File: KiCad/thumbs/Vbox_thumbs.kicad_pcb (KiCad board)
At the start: 2 copper layers, 33.1 x 114.3 mm, 4 parts, among them J4 Conn_01x06, J5 Conn_01x06, J6 Conn_01x10, J7 Conn_01x10

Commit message: thumbs and fingers
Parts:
- removed J4, J5: Conn_01x06, Connector_JST:JST_PH_S6B-PH-SM4-TB_1x06-1MP_P2.00mm_Horizontal
- removed J6, J7: Conn_01x10, Connector_JST:JST_PH_S10B-PH-SM4-TB_1x10-1MP_P2.00mm_Horizontal
- added J1: Conn_01x06, Connector_JST:JST_PH_S6B-PH-SM4-TB_1x06-1MP_P2.00mm_Horizontal, F.Cu at (85.2, 108.0)
- added J2: Conn_01x06, Connector_JST:JST_PH_S6B-PH-SM4-TB_1x06-1MP_P2.00mm_Horizontal, B.Cu at (85.2, 108.0)
- added SW1: SW_Push_45deg, Buttons:Vbox, F.Cu at (119.0, 109.5)
- added SW10: SW_Push_45deg, Buttons:Vbox, B.Cu at (138.0, 119.0)
- added SW2: SW_Push_45deg, Buttons:Vbox, F.Cu at (100.0, 100.0)
- added SW3: SW_Push_45deg, Buttons:Vbox, F.Cu at (119.0, 90.5)
- added SW4: SW_Push_45deg, Buttons:Vbox, F.Cu at (138.0, 100.0)
- added SW5: SW_Push_45deg, Buttons:Vbox, F.Cu at (138.0, 119.0)
- added SW6: SW_Push_45deg, Buttons:Vbox, B.Cu at (119.0, 109.5)
- added SW7: SW_Push_45deg, Buttons:Vbox, B.Cu at (100.0, 100.0)
- added SW8: SW_Push_45deg, Buttons:Vbox, B.Cu at (119.0, 90.5)
- added SW9: SW_Push_45deg, Buttons:Vbox, B.Cu at (138.0, 100.0)
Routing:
- net C_UP: track 0.00 -> 86.0 mm
- net C_DN: track 0.00 -> 65.7 mm
- net C_LT: track 0.00 -> 58.8 mm
- net M2: track 0.00 -> 56.2 mm
- net M3: track 0.00 -> 52.6 mm
- net M4: track 0.00 -> 44.7 mm
- net A: track 0.00 -> 33.8 mm
- net M1: track 0.00 -> 31.3 mm
- net C_RT: track 0.00 -> 17.0 mm
- net M5: track 0.00 -> 12.9 mm
- net GND: vias 32 -> 12
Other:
- board size 33.1 x 114.3 mm -> 67 x 46.5 mm

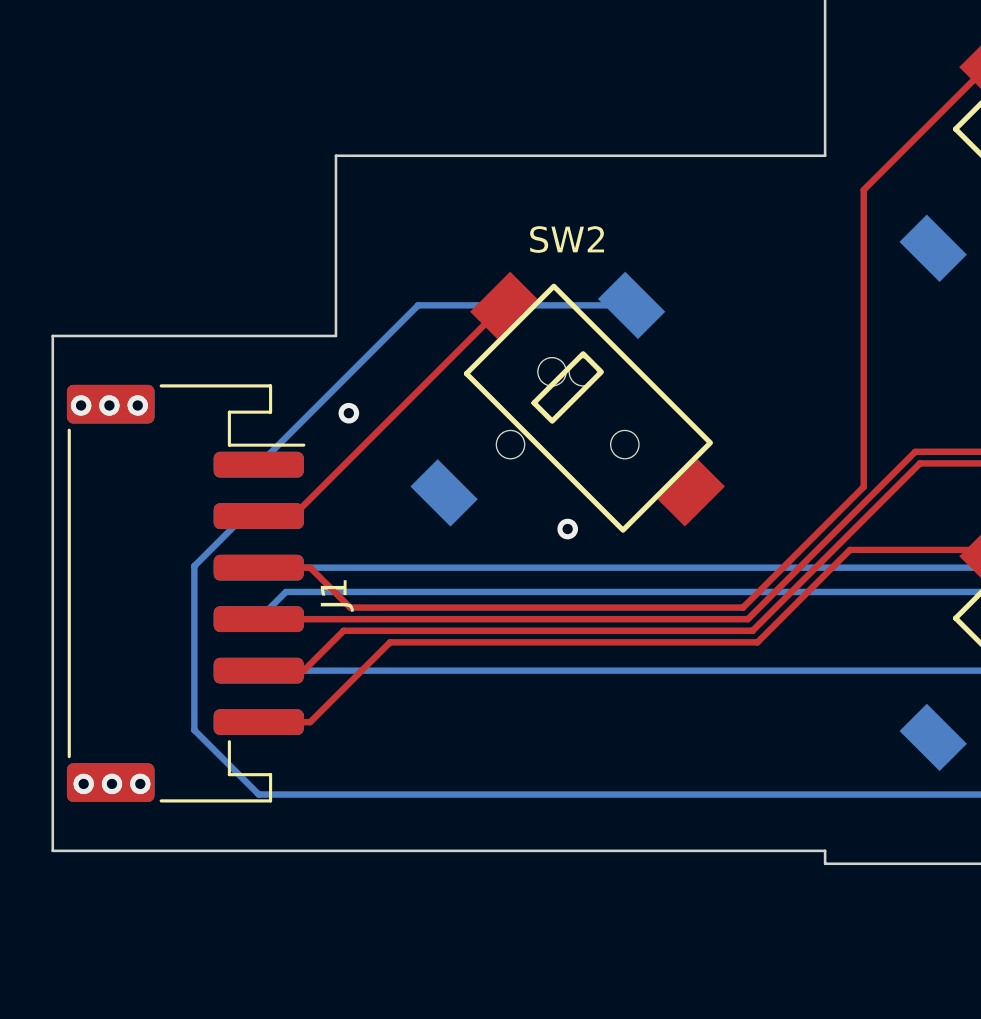
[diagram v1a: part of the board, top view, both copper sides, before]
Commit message: tweak outlines of button clusters
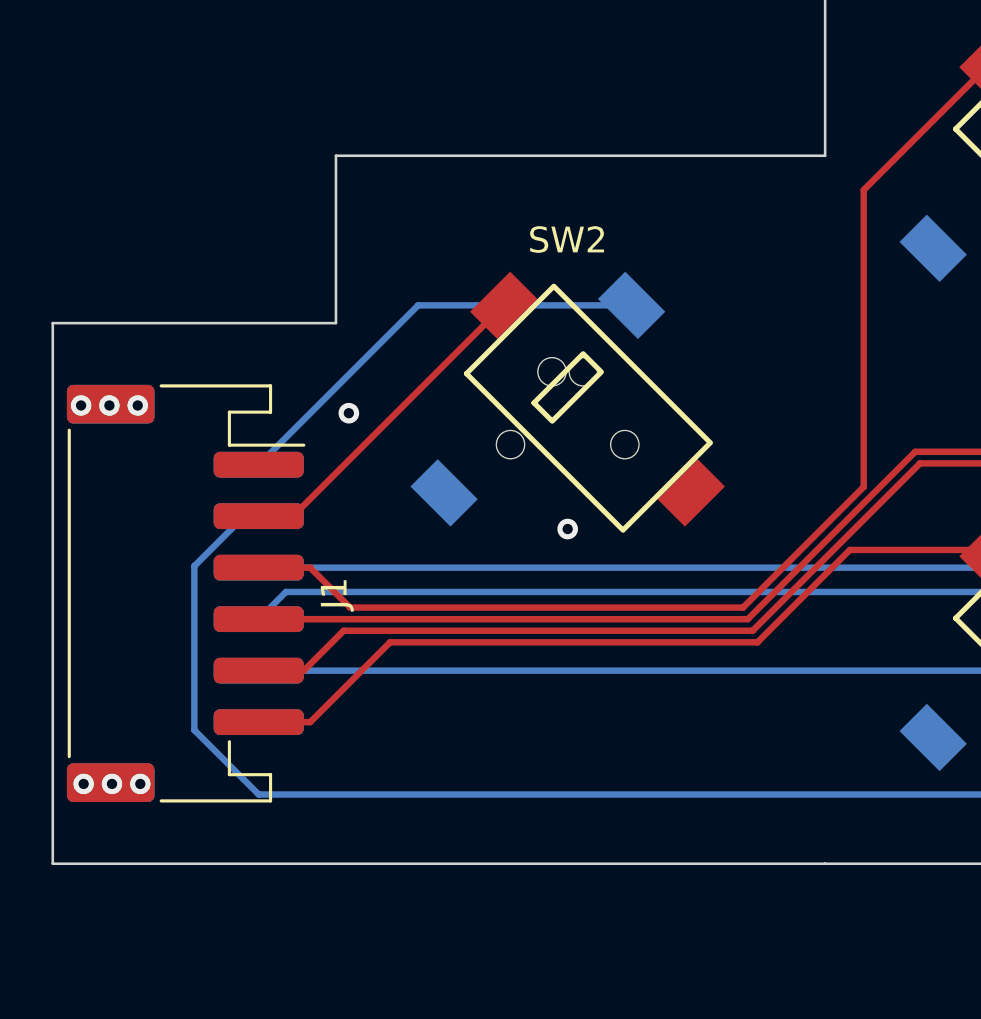
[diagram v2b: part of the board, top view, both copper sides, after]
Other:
- outline, holes or cut-outs redrawn
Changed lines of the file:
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@@
   (gr_poly
     (pts
-      (xy 80 118)
-      (xy 110 118)
+      (xy 80 118.5)
       (xy 110 118.5)
       (xy 129 118.5)
@@
       (xy 110 91)
       (xy 91 91)
-      (xy 91 98)
-      (xy 80 98)
+      (xy 91 97.5)
+      (xy 80 97.5)
     )
     (stroke (width 0.1) (type solid)) (fill none) (layer "Edge.Cuts"))
   (gr_text_box "VBox Thumb Cluster\nby CarVac\nLicense: CERN-OHL-S V2\ngithub.com/CarVac/vbox"
-    (start 90.5 109.5) (end 109.5 118) (layer "F.SilkS")
+    (start 90.5 111) (end 109.5 117.5) (layer "F.SilkS")
       (effects (font (size 0.8 0.8) (thickness 0.15)) (justify top))
   )
@@
     (polygon
       (pts
-        (xy 80 118)
-        (xy 110 118)
+        (xy 80 118.5)
         (xy 110 118.5)
         (xy 129 118.5)
@@
         (xy 110 91)
         (xy 91 91)
-        (xy 91 98)
-        (xy 80 98)
+        (xy 91 97.5)
+        (xy 80 97.5)
       )
     )
@@
     (polygon
       (pts
-        (xy 80 118)
-        (xy 110 118)
+        (xy 80 118.5)
         (xy 110 118.5)
         (xy 129 118.5)
@@
         (xy 110 91)
         (xy 91 91)
-        (xy 91 98)
-        (xy 80 98)
+        (xy 91 97.5)
+        (xy 80 97.5)
       )
     )

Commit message: fix drc errors
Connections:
- J2 pad 1: GND -> C_RT
- J2 pad 2: C_UP -> C_DN
- J2 pad 3: C_LT -> A
- J2 pad 4: A -> C_LT
- J2 pad 5: C_DN -> C_UP
- J2 pad 6: C_RT -> GND
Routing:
- net C_UP: track 86.0 -> 48.4 mm
- net C_RT: track 17.0 -> 33.2 mm
- net C_DN: track 65.7 -> 55.1 mm
- net C_LT: track 58.8 -> 56.7 mm
- net A: track 33.8 -> 34.6 mm
- net GND: vias 12 -> 11

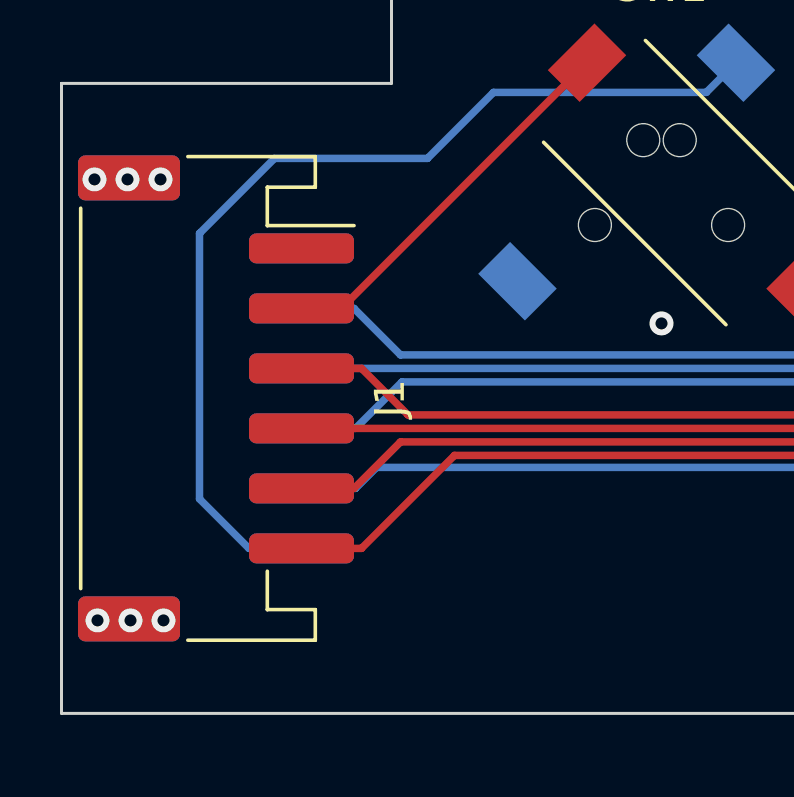
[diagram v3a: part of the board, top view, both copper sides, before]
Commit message: add thermal clearances to fingers, a few more vias
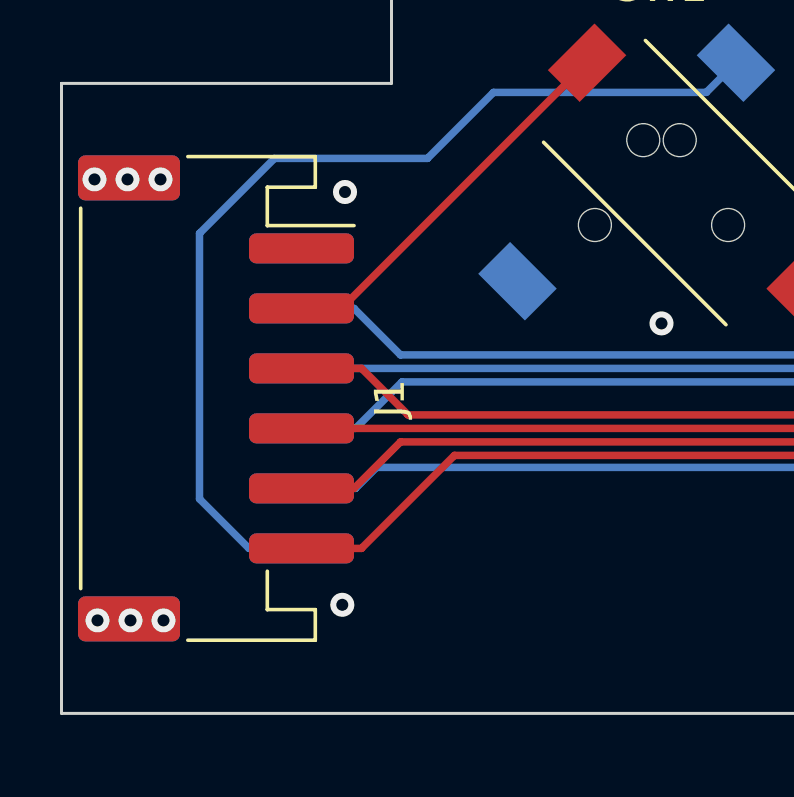
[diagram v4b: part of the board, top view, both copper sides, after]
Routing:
- net GND: vias 11 -> 13
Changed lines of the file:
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@@
       (net 4 "M5") (pinfunction "1") (pintype "passive"))
     (pad "2" smd rect (at 4.801256 4.094149 45) (size 2.2 1.5) (layers "F.Cu" "F.Paste" "F.Mask")
-      (net 1 "GND") (pinfunction "2") (pintype "passive"))
+      (net 1 "GND") (pinfunction "2") (pintype "passive") (thermal_gap 1))
   )
   (footprint "Buttons:Vbox" (layer "F.Cu")
@@
       (net 2 "M3") (pinfunction "1") (pintype "passive"))
     (pad "2" smd rect (at 4.801256 4.094149 45) (size 2.2 1.5) (layers "F.Cu" "F.Paste" "F.Mask")
-      (net 1 "GND") (pinfunction "2") (pintype "passive"))
+      (net 1 "GND") (pinfunction "2") (pintype "passive") (thermal_gap 1))
   )
   (footprint "Buttons:Vbox" (layer "F.Cu")
@@
       (net 5 "M1") (pinfunction "1") (pintype "passive"))
     (pad "2" smd rect (at 4.801256 4.094149 45) (size 2.2 1.5) (layers "F.Cu" "F.Paste" "F.Mask")
-      (net 1 "GND") (pinfunction "2") (pintype "passive"))
+      (net 1 "GND") (pinfunction "2") (pintype "passive") (thermal_gap 1))
   )
   (footprint "Buttons:Vbox" (layer "F.Cu")
@@
       (net 3 "M4") (pinfunction "1") (pintype "passive"))
     (pad "2" smd rect (at 4.801256 4.094149 45) (size 2.2 1.5) (layers "F.Cu" "F.Paste" "F.Mask")
-      (net 1 "GND") (pinfunction "2") (pintype "passive"))
+      (net 1 "GND") (pinfunction "2") (pintype "passive") (thermal_gap 1))
   )
   (footprint "Buttons:Vbox" (layer "F.Cu")
@@
       (net 6 "M2") (pinfunction "1") (pintype "passive"))
     (pad "2" smd rect (at 4.801256 4.094149 45) (size 2.2 1.5) (layers "F.Cu" "F.Paste" "F.Mask")
-      (net 1 "GND") (pinfunction "2") (pintype "passive"))
+      (net 1 "GND") (pinfunction "2") (pintype "passive") (thermal_gap 1))
   )
   (footprint "Connector_JST:JST_PH_S6B-PH-SM4-TB_1x06-1MP_P2.00mm_Horizontal" (layer "F.Cu")
@@
       (stroke (width 0.1) (type solid)) (layer "F.Fab"))
     (pad "1" smd roundrect (at -5 -2.85 270) (size 1 3.5) (layers "F.Cu" "F.Paste" "F.Mask") (roundrect_rratio 0.25)
-      (net 1 "GND") (pinfunction "Pin_1") (pintype "passive"))
+      (net 1 "GND") (pinfunction "Pin_1") (pintype "passive") (thermal_bridge_width 0.2) (thermal_gap 0.7))
     (pad "2" smd roundrect (at -3 -2.85 270) (size 1 3.5) (layers "F.Cu" "F.Paste" "F.Mask") (roundrect_rratio 0.25)
       (net 4 "M5") (pinfunction "Pin_2") (pintype "passive"))
@@
       (net 5 "M1") (pinfunction "Pin_6") (pintype "passive"))
     (pad "MP" smd roundrect (at -7.35 2.9 270) (size 1.5 3.4) (layers "F.Cu" "F.Paste" "F.Mask") (roundrect_rratio 0.166667)
-      (net 1 "GND"))
+      (net 1 "GND") (thermal_gap 1))
     (pad "MP" smd roundrect (at 7.35 2.9 270) (size 1.5 3.4) (layers "F.Cu" "F.Paste" "F.Mask") (roundrect_rratio 0.166667)
-      (net 1 "GND"))
+      (net 1 "GND") (thermal_gap 1))
     (model "${KICAD6_3DMODEL_DIR}/Connector_JST.3dshapes/JST_PH_S6B-PH-SM4-TB_1x06-1MP_P2.00mm_Horizontal.wrl"
       (offset (xyz 0 0 0))
@@
       (net 8 "C_LT") (pinfunction "1") (pintype "passive"))
     (pad "2" smd rect (at 4.801256 -4.094149 135) (size 2.2 1.5) (layers "B.Cu" "B.Paste" "B.Mask")
-      (net 1 "GND") (pinfunction "2") (pintype "passive"))
+      (net 1 "GND") (pinfunction "2") (pintype "passive") (thermal_gap 1))
   )
   (footprint "Buttons:Vbox" (layer "B.Cu")
@@
       (net 11 "C_RT") (pinfunction "1") (pintype "passive"))
     (pad "2" smd rect (at 4.801256 -4.094149 135) (size 2.2 1.5) (layers "B.Cu" "B.Paste" "B.Mask")
-      (net 1 "GND") (pinfunction "2") (pintype "passive"))
+      (net 1 "GND") (pinfunction "2") (pintype "passive") (thermal_bridge_angle 45) (thermal_gap 1))
   )
   (footprint "Buttons:Vbox" (layer "B.Cu")
@@
       (net 9 "A") (pinfunction "1") (pintype "passive"))
     (pad "2" smd rect (at 4.801256 -4.094149 135) (size 2.2 1.5) (layers "B.Cu" "B.Paste" "B.Mask")
-      (net 1 "GND") (pinfunction "2") (pintype "passive"))
+      (net 1 "GND") (pinfunction "2") (pintype "passive") (thermal_gap 1))
   )
   (footprint "Connector_JST:JST_PH_S6B-PH-SM4-TB_1x06-1MP_P2.00mm_Horizontal" (layer "B.Cu")
@@
       (net 7 "C_UP") (pinfunction "Pin_5") (pintype "passive"))
     (pad "6" smd roundrect (at 5 2.85 90) (size 1 3.5) (layers "B.Cu" "B.Paste" "B.Mask") (roundrect_rratio 0.25)
-      (net 1 "GND") (pinfunction "Pin_6") (pintype "passive"))
+      (net 1 "GND") (pinfunction "Pin_6") (pintype "passive") (thermal_bridge_width 0.2) (thermal_gap 0.7))
     (pad "MP" smd roundrect (at -7.35 -2.9 90) (size 1.5 3.4) (layers "B.Cu" "B.Paste" "B.Mask") (roundrect_rratio 0.166667)
-      (net 1 "GND"))
+      (net 1 "GND") (thermal_gap 1))
     (pad "MP" smd roundrect (at 7.35 -2.9 90) (size 1.5 3.4) (layers "B.Cu" "B.Paste" "B.Mask") (roundrect_rratio 0.166667)
-      (net 1 "GND"))
+      (net 1 "GND") (thermal_gap 1))
     (model "${KICAD6_3DMODEL_DIR}/Connector_JST.3dshapes/JST_PH_S6B-PH-SM4-TB_1x06-1MP_P2.00mm_Horizontal.wrl"
       (offset (xyz 0 0 0))
@@
       (net 10 "C_DN") (pinfunction "1") (pintype "passive"))
     (pad "2" smd rect (at 4.801256 -4.094149 135) (size 2.2 1.5) (layers "B.Cu" "B.Paste" "B.Mask")
-      (net 1 "GND") (pinfunction "2") (pintype "passive"))
+      (net 1 "GND") (pinfunction "2") (pintype "passive") (thermal_gap 1))
   )
   (footprint "Buttons:Vbox" (layer "B.Cu")
@@
       (net 7 "C_UP") (pinfunction "1") (pintype "passive"))
     (pad "2" smd rect (at 4.801256 -4.094149 135) (size 2.2 1.5) (layers "B.Cu" "B.Paste" "B.Mask")
-      (net 1 "GND") (pinfunction "2") (pintype "passive"))
+      (net 1 "GND") (pinfunction "2") (pintype "passive") (thermal_gap 1))
   )
   (gr_poly
@@
   (via (at 81.2 115.4) (size 0.8) (drill 0.4) (layers "F.Cu" "B.Cu") (net 1))
   (via (at 100 105.5) (size 0.8) (drill 0.4) (layers "F.Cu" "B.Cu") (free) (net 1))
+  (via (at 89.45 101.12) (size 0.8) (drill 0.4) (layers "F.Cu" "B.Cu") (free) (net 1))
   (via (at 138 105) (size 0.8) (drill 0.4) (layers "F.Cu" "B.Cu") (free) (net 1))
   (via (at 83.4 115.4) (size 0.8) (drill 0.4) (layers "F.Cu" "B.Cu") (net 1))
   (via (at 119 96) (size 0.8) (drill 0.4) (layers "F.Cu" "B.Cu") (free) (net 1))
   (via (at 138 124.5) (size 0.8) (drill 0.4) (layers "F.Cu" "B.Cu") (free) (net 1))
+  (via (at 89.36 114.88) (size 0.8) (drill 0.4) (layers "F.Cu" "B.Cu") (free) (net 1))
   (via (at 83.3 100.7) (size 0.8) (drill 0.4) (layers "F.Cu" "B.Cu") (net 1))
   (via (at 82.3 115.4) (size 0.8) (drill 0.4) (layers "F.Cu" "B.Cu") (net 1))

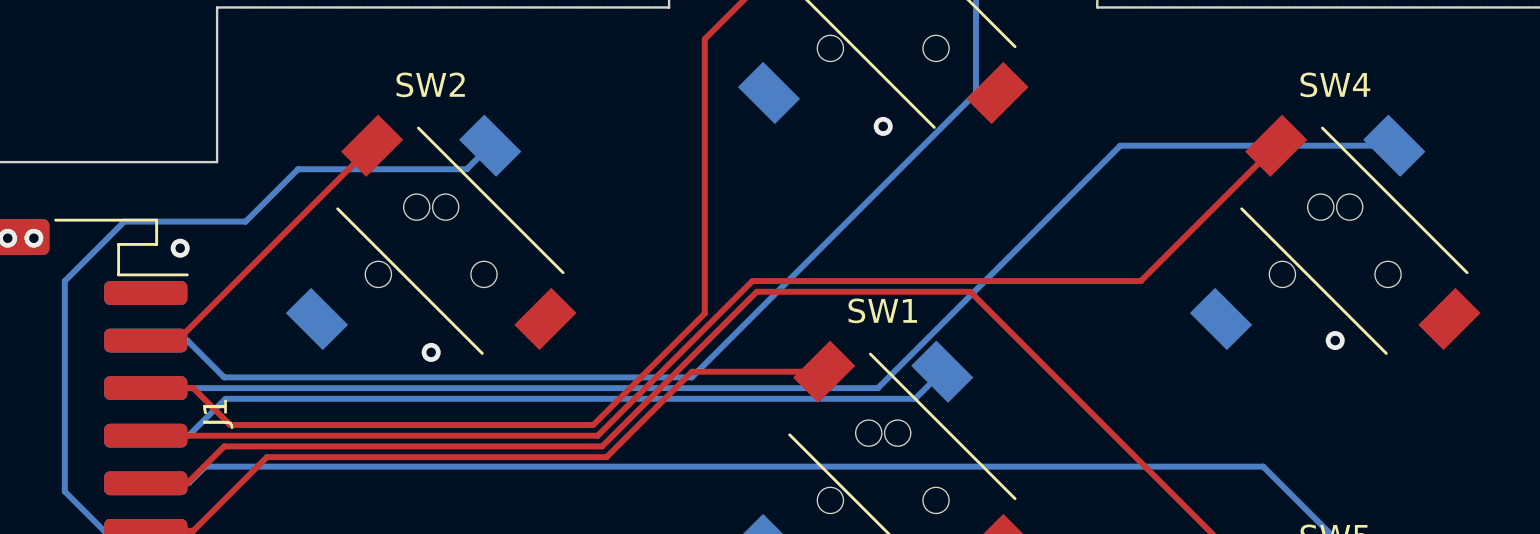
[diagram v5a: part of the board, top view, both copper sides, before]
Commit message: move traces away from hand solder pads
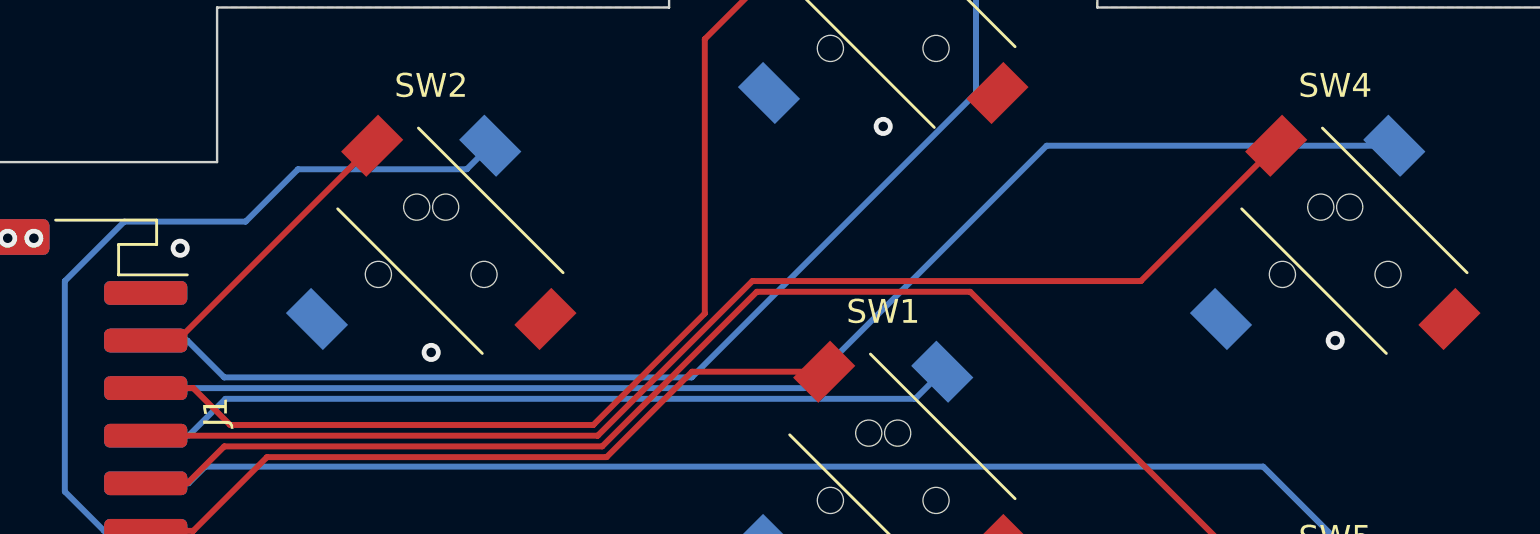
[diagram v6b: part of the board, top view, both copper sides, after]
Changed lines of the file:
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@@
   (segment (start 110.95 106.55) (end 122.9 94.6) (width 0.25) (layer "B.Cu") (net 7))
   (segment (start 122.9 94.6) (end 122.9 88.729005) (width 0.25) (layer "B.Cu") (net 7))
-  (segment (start 128.966688 96.810949) (end 140.481944 96.810949) (width 0.25) (layer "B.Cu") (net 8))
-  (segment (start 118.777637 107) (end 128.966688 96.810949) (width 0.25) (layer "B.Cu") (net 8))
-  (segment (start 88 107) (end 118.777637 107) (width 0.25) (layer "B.Cu") (net 8))
+  (segment (start 115.68 107) (end 125.869051 96.810949) (width 0.25) (layer "B.Cu") (net 8))
+  (segment (start 125.869051 96.810949) (end 140.481944 96.810949) (width 0.25) (layer "B.Cu") (net 8))
+  (segment (start 88 107) (end 115.68 107) (width 0.25) (layer "B.Cu") (net 8))
   (segment (start 89.8 109) (end 91.35 107.45) (width 0.25) (layer "B.Cu") (net 9))
   (segment (start 88 109) (end 89.8 109) (width 0.25) (layer "B.Cu") (net 9))
